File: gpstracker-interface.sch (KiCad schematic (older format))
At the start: 13 parts, among them J1 Molex 105133-0002, U6 FT231XS

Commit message: Fixed references for 4.7uF capacitor
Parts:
- C10: Manufacturer part number C0805X475C4RACTU -> C0805X475J4RACAUTO
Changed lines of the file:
@@
 F 3 "" H 1300 1550 50  0001 C CNN
 F 4 "Kemet" H 1300 1550 60  0001 C CNN "Manufacturer"
-F 5 "C0805X475C4RACTU" H 1300 1550 60  0001 C CNN "Manufacturer part number"
+F 5 "C0805X475J4RACAUTO" H 1300 1550 60  0001 C CNN "Manufacturer part number"
 F 6 "0805" H 1300 1550 60  0001 C CNN "Package"
 	1    1300 1550

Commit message: Replaced USB connector by Wuerth one
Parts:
- J1: footprint custom-conn:USB_Micro-B_Vertical_Molex-105133-0001_HandSoldering -> Connectors_USB:USB_Micro-B_Wuerth-614105150721_Vertical_CircularHoles; Manufacturer Molex -> (none); Manufacturer part number 105133-0002 -> 614105150721; Wuerth (none) -> Molex
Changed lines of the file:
@@
 F 0 "J1" H 900 1450 50  0000 L CNN
 F 1 "Molex 105133-0002" H 900 1350 50  0001 L CNN
-F 2 "custom-conn:USB_Micro-B_Vertical_Molex-105133-0001_HandSoldering" H 1250 950 50  0001 C CNN
+F 2 "Connectors_USB:USB_Micro-B_Wuerth-614105150721_Vertical_CircularHoles" H 1250 950 50  0001 C CNN
 F 3 "" H 1250 950 50  0001 C CNN
-F 4 "Molex" H 1100 1000 60  0001 C CNN "Manufacturer"
-F 5 "105133-0002" H 1100 1000 60  0001 C CNN "Manufacturer part number"
+F 4 "Molex" H 1100 1000 60  0001 C CNN "Wuerth"
+F 5 "614105150721" H 1100 1000 60  0001 C CNN "Manufacturer part number"
 	1    1100 1000
 	0    1    1    0

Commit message: Update BOM and added some vias
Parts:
- J1: Manufacturer (none) -> Wuerth; Wuerth Molex -> (none)
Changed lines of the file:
@@
 F 2 "Connectors_USB:USB_Micro-B_Wuerth-614105150721_Vertical_CircularHoles" H 1250 950 50  0001 C CNN
 F 3 "" H 1250 950 50  0001 C CNN
-F 4 "Molex" H 1100 1000 60  0001 C CNN "Wuerth"
+F 4 "Wuerth" H 1100 1000 60  0001 C CNN "Manufacturer"
 F 5 "614105150721" H 1100 1000 60  0001 C CNN "Manufacturer part number"
 	1    1100 1000

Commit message: Updated schematics references with updated and available parts. This is the version that was ordered on Mouser/Seeedstudio
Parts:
- C10: Manufacturer part number C0805X475J4RACAUTO -> C0805C104M3RACTU
- C11, C13: Manufacturer Kemet -> Vishay; Manufacturer part number C0805X475C4RACTU -> VJ0805A470GXJPW1BC
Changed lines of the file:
@@
 F 2 "Capacitors_SMD:C_0805_HandSoldering" H 1388 2150 50  0001 C CNN
 F 3 "" H 1350 2300 50  0001 C CNN
-F 4 "Kemet" H 1350 2300 60  0001 C CNN "Manufacturer"
-F 5 "C0805X475C4RACTU" H 1350 2300 60  0001 C CNN "Manufacturer part number"
+F 4 "Vishay" H 1350 2300 60  0001 C CNN "Manufacturer"
+F 5 "VJ0805A470GXJPW1BC" H 1350 2300 60  0001 C CNN "Manufacturer part number"
 F 6 "0805" H 1350 2300 60  0001 C CNN "Package"
 	1    1350 2300
@@
 F 2 "Capacitors_SMD:C_0805_HandSoldering" H 1038 2150 50  0001 C CNN
 F 3 "" H 1000 2300 50  0001 C CNN
-F 4 "Kemet" H 1000 2300 60  0001 C CNN "Manufacturer"
-F 5 "C0805X475C4RACTU" H 1000 2300 60  0001 C CNN "Manufacturer part number"
+F 4 "Vishay" H 1000 2300 60  0001 C CNN "Manufacturer"
+F 5 "VJ0805A470GXJPW1BC" H 1000 2300 60  0001 C CNN "Manufacturer part number"
 F 6 "0805" H 1000 2300 60  0001 C CNN "Package"
 	1    1000 2300
@@
 F 3 "" H 1300 1550 50  0001 C CNN
 F 4 "Kemet" H 1300 1550 60  0001 C CNN "Manufacturer"
-F 5 "C0805X475J4RACAUTO" H 1300 1550 60  0001 C CNN "Manufacturer part number"
+F 5 "C0805C104M3RACTU" H 1300 1550 60  0001 C CNN "Manufacturer part number"
 F 6 "0805" H 1300 1550 60  0001 C CNN "Package"
 	1    1300 1550

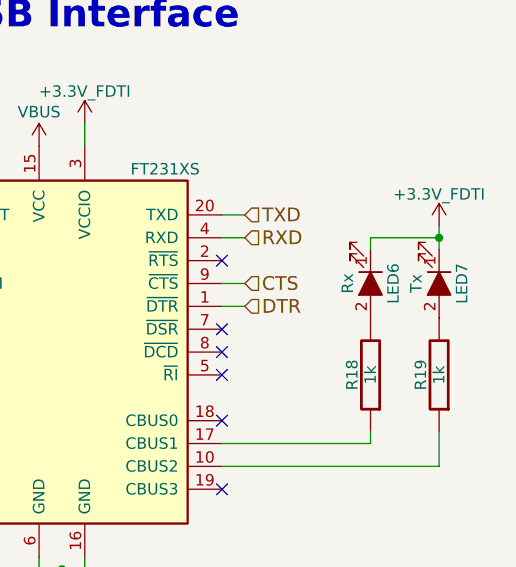
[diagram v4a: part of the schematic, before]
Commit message: Fixed LED6 & LED7 being polarity reversed
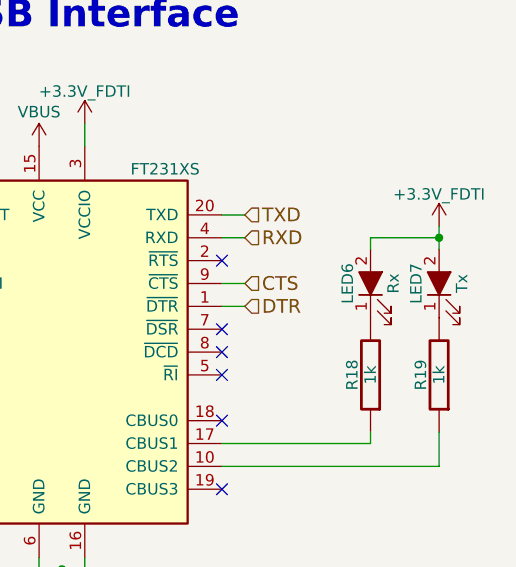
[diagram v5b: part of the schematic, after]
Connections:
- net +3V3_FDTI: now also LED6.2 (A), LED7.2 (A); no longer LED6.1 (K), LED7.1 (K)
- net at R18.2: now also LED6.1 (K); no longer LED6.2 (A)
- net at R19.2: now also LED7.1 (K); no longer LED7.2 (A)
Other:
- moved on the sheet: LED6, LED7
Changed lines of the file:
@@
 F 6 "0805" H 4150 2000 60  0001 C CNN "Package"
 	1    4150 2000
-	0    1    1    0
+	0    -1   -1   0
 $EndComp
 $Comp
@@
 F 6 "0805" H 4450 2000 60  0001 C CNN "Package"
 	1    4450 2000
-	0    1    1    0
+	0    -1   -1   0
 $EndComp
 $Comp
